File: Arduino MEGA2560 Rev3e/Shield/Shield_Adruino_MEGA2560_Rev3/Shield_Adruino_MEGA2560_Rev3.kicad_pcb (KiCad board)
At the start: 2 copper layers, 101.6 x 53.3 mm, 16 parts

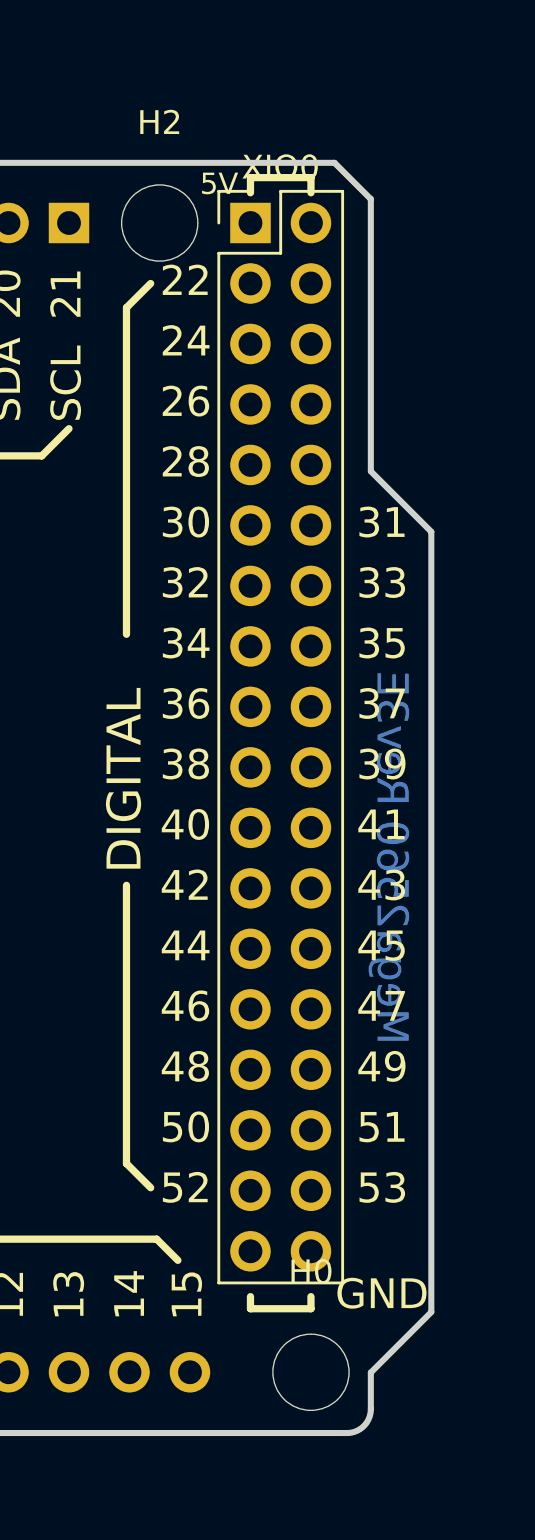
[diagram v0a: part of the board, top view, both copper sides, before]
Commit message: Update Shield_Adruino_MEGA2560_Rev3.kicad_pcb, Shield_Adruino_MEGA2560_Rev3.kicad_pro, and Shield_Adruino_MEGA2560_Rev3.kicad_sch to KiCad 7
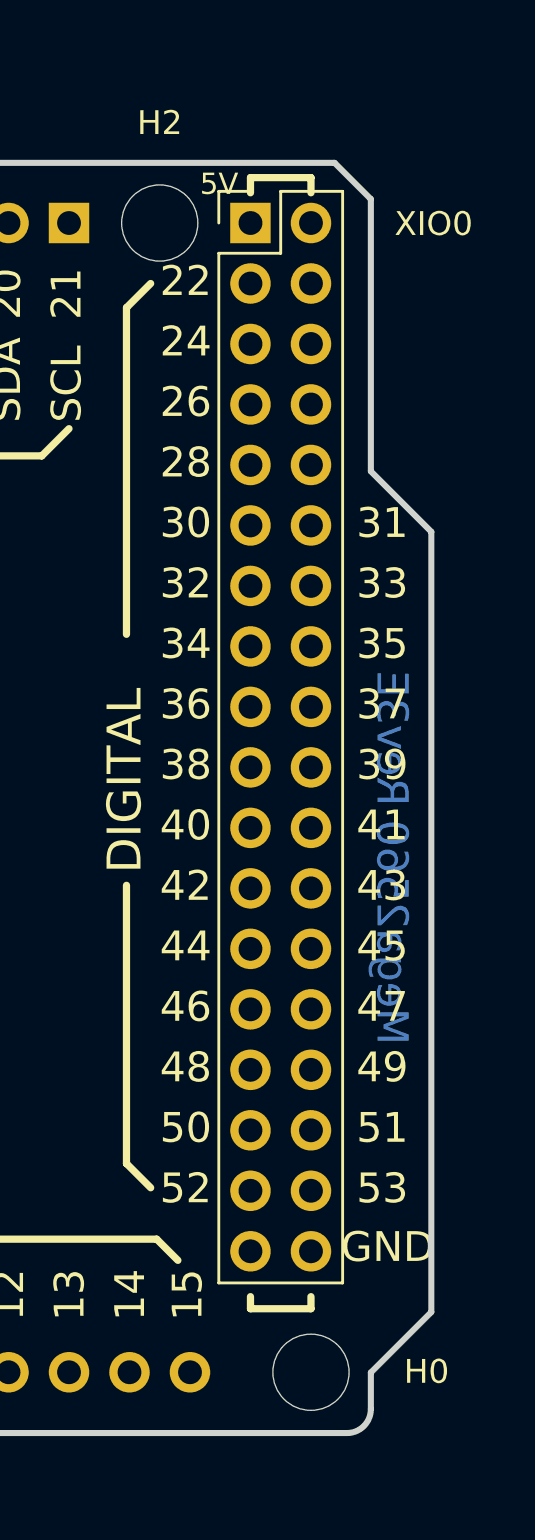
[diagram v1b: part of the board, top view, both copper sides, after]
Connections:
- COMMUNICATION0 pad 3: /RXD1 -> (no net)
- COMMUNICATION0 pad 4: /TXD1 -> (no net)
- COMMUNICATION0 pad 5: /RXD2 -> (no net)
- COMMUNICATION0 pad 6: /TXD2 -> (no net)
- COMMUNICATION0 pad 7: /RXD3 -> (no net)
- COMMUNICATION0 pad 8: /TXD3 -> (no net)
- JP6 pad 10: /PH5 -> (no net)
- JP6 pad 5: /PB7 -> (no net)
- JP6 pad 6: /PB6 -> (no net)
- JP6 pad 7: /PB5 -> (no net)
- JP6 pad 8: /PB4 -> (no net)
- JP6 pad 9: /PH6 -> (no net)
- POWER0 pad 1: unconnected-(POWER0-Pad1) -> (no net)
- PWML0 pad 1: /PE0 -> (no net)
- PWML0 pad 2: /PE1 -> (no net)
- PWML0 pad 3: /PE4 -> (no net)
- PWML0 pad 4: /PE5 -> (no net)
- PWML0 pad 5: /PG5 -> (no net)
- PWML0 pad 6: /PE3 -> (no net)
- PWML0 pad 7: /PH3 -> (no net)
- PWML0 pad 8: /PH4 -> (no net)
- XIO0 pad 10: /PA7 -> (no net)
- XIO0 pad 11: /PC7 -> (no net)
- XIO0 pad 12: /PC6 -> (no net)
- XIO0 pad 13: /PC5 -> (no net)
- XIO0 pad 14: /PC4 -> (no net)
- XIO0 pad 15: /PC3 -> (no net)
- XIO0 pad 16: /PC2 -> (no net)
- XIO0 pad 17: /PC1 -> (no net)
- XIO0 pad 18: /PC0 -> (no net)
- XIO0 pad 19: /PD7 -> (no net)
- XIO0 pad 20: /PG2 -> (no net)
- XIO0 pad 21: /PG1 -> (no net)
- XIO0 pad 22: /PG0 -> (no net)
- XIO0 pad 23: /PL7 -> (no net)
- XIO0 pad 24: /PL6 -> (no net)
- XIO0 pad 25: /PL5 -> (no net)
- XIO0 pad 26: /PL4 -> (no net)
- XIO0 pad 27: /PL3 -> (no net)
- XIO0 pad 28: /PL2 -> (no net)
- XIO0 pad 29: /PL1 -> (no net)
- XIO0 pad 3: /PA0 -> (no net)
- XIO0 pad 30: /PL0 -> (no net)
- XIO0 pad 31: /PB3 -> (no net)
- XIO0 pad 32: /PB2 -> (no net)
- XIO0 pad 33: /PB1 -> (no net)
- XIO0 pad 34: /PB0 -> (no net)
- XIO0 pad 4: /PA1 -> (no net)
- XIO0 pad 5: /PA2 -> (no net)
- XIO0 pad 6: /PA3 -> (no net)
- XIO0 pad 7: /PA4 -> (no net)
- XIO0 pad 8: /PA5 -> (no net)
- XIO0 pad 9: /PA6 -> (no net)
